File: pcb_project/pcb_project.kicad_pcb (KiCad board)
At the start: 8 copper layers, 238 parts, among them IC1 TPS54325PWPR, IC2 TPS54294PWPR, IC3 IS61WV204816BLL-10TLI, IC4 IS61WV204816BLL-10TLI, J1 Conn_01x10_Pin, J10 M20-9990246, J11 M20-9990246, J12 M20-9990246, J2 FTSH-107-01-F-DV-K, J3 Conn_ST_STDC14, J4 DE15_Socket_HighDensity_Mount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, J5 USB_B_Micro, J6 MEM2052-00-195-00-A, J7 USB_A, J8 M20-9990246, J9 M20-9990246, Q1 BC857BS, Q2 BC847BPN, SW2 SW_SPDT, SW3 SW_SPST, SW4 SW_SPST, U1 XC7A100T-FTG256, U2 STM32U595VJTx, U3 TPS2041B, U4 D3V3XA4B10LP, U7 MAX7221xWG, U8 COM-11405, U9 MT25QL128ABA1ESE-0SIT, Y1 48MHz, Y2 XLH736025.175000I

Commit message: Initial FPGA ballout and vga
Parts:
- C10, C100, C101, C102, C11, C13, C19, C20, C22, C23, C24, C25, C27, C29, C31, C33, C34, C36, C5, C8, C92, C93, C94, C95, C99: footprint Capacitor_SMD:C_0805_2012Metric_Pad1.18x1.45mm_HandSolder -> Capacitor_SMD:C_0603_1608Metric_Pad1.08x0.95mm_HandSolder
- C6: footprint Capacitor_SMD:CP_Elec_10x10.5 -> Capacitor_Tantalum_SMD:CP_EIA-7343-31_Kemet-D_HandSolder
- moved U9 40.8 mm to (86.5, 137.5)
- moved C10 40.2 mm to (64.5, 107.0)
- moved C13 40.2 mm to (69.3, 98.0)
- moved C17 40.2 mm to (69.3, 107.0)
- moved C20 40.2 mm to (74.1, 98.0)
- moved C24 40.2 mm to (74.1, 107.0)
- moved C5 40.2 mm to (64.5, 98.0)
- moved C29 40.2 mm to (78.9, 98.0)
- moved C11 40.2 mm to (69.3, 92.0)
- moved C15 40.2 mm to (69.3, 101.0)
- moved C18 40.2 mm to (74.1, 92.0)
- moved C22 40.2 mm to (74.1, 101.0)
- moved C3 40.2 mm to (64.5, 92.0)
- moved C8 40.2 mm to (64.5, 101.0)
- moved C12 40.2 mm to (69.3, 95.0)
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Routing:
- net /VGA/R0: track 0.00 -> 103.1 mm, vias 0 -> 2
- net /VGA/R1: track 0.00 -> 98.2 mm, vias 0 -> 1
- net /VGA/R2: track 0.00 -> 97.4 mm, vias 0 -> 1
- net /VGA/R3: track 0.00 -> 96.0 mm, vias 0 -> 1
- net /VGA/R4: track 0.00 -> 94.9 mm, vias 0 -> 2
- net /VGA/B3: track 0.00 -> 56.7 mm
- net /VGA/G0: track 0.00 -> 38.2 mm
- net /VGA/B2: track 0.00 -> 36.2 mm
- net /VGA/G1: track 0.00 -> 34.8 mm
- net /VGA/B1: track 0.00 -> 33.5 mm, vias 0 -> 2
- net /VGA/G2: track 0.00 -> 32.8 mm
- net /VGA/G3: track 0.00 -> 32.0 mm
- net /VGA/G4: track 0.00 -> 29.5 mm
- net /VGA/B0: track 0.00 -> 29.4 mm
- net /VGA/G5: track 0.00 -> 28.8 mm
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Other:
- copper layers 8 -> 6

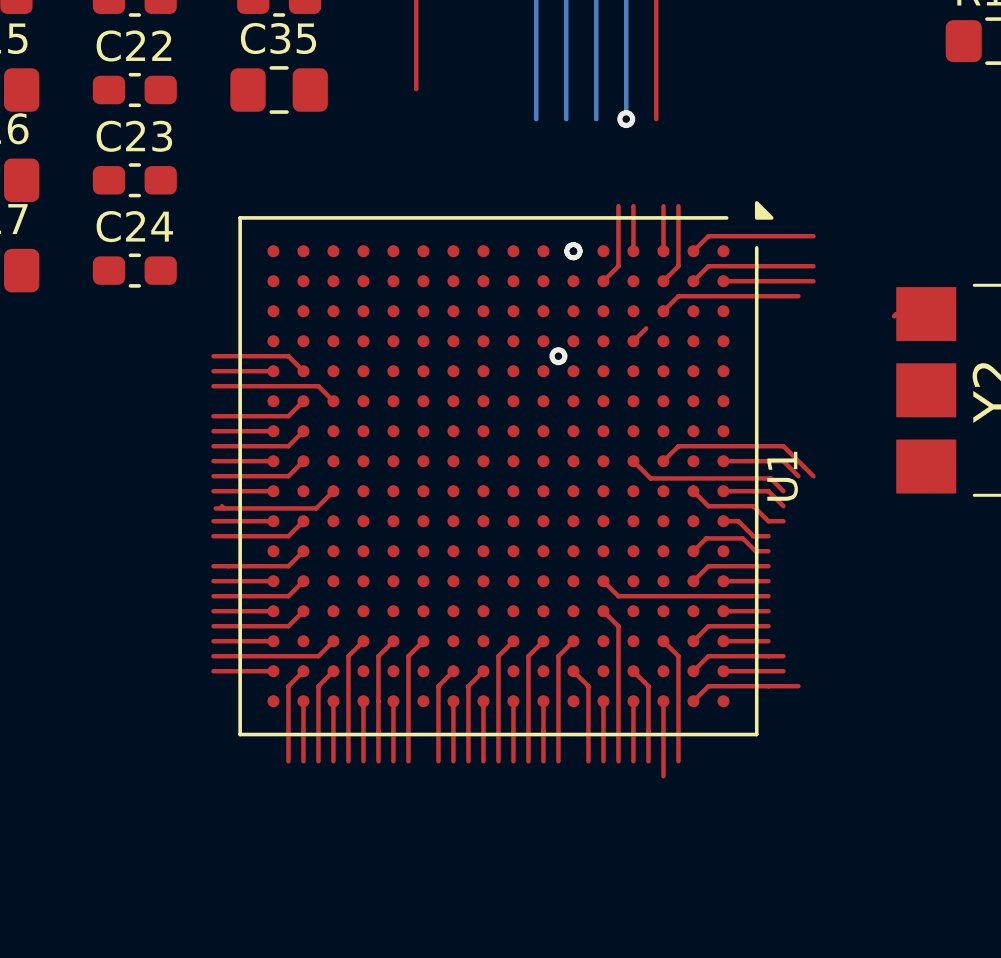
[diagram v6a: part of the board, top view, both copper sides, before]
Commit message: FPGA Dog Bone wires
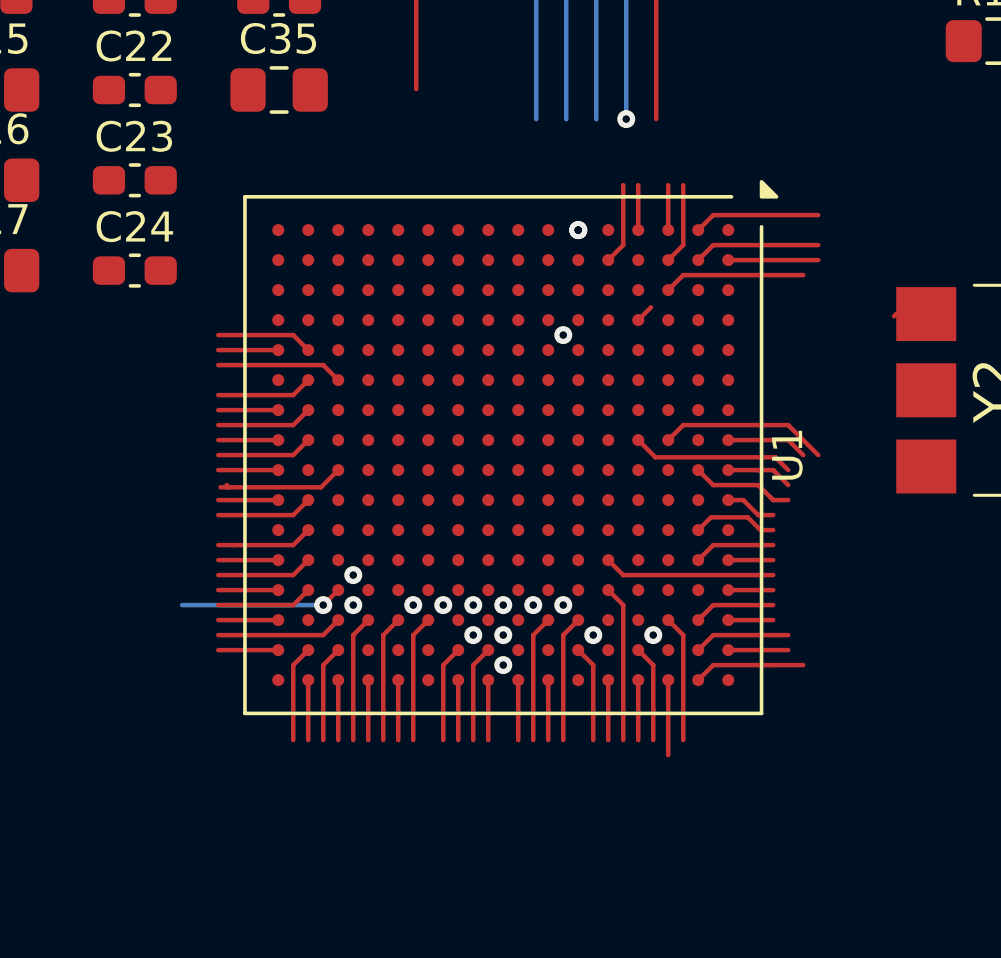
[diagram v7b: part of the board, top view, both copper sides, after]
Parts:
- moved U1 0.72 mm to (86.4, 113.2)
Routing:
- net Net-(IC4-I/O4): track 0.21 -> 5.49 mm, vias 0 -> 1
- net Net-(IC3-I/O15): track 4.21 -> 0.00 mm
- net (no net): vias 1 -> 14

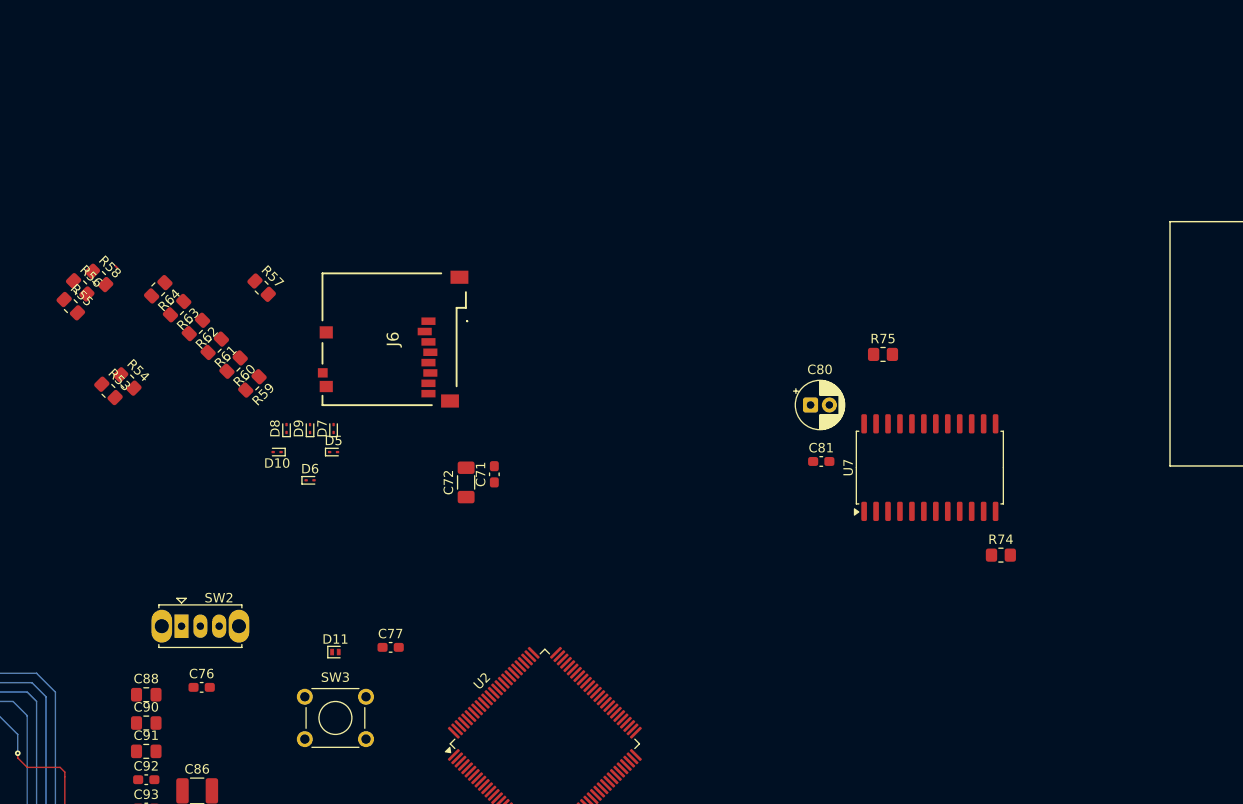
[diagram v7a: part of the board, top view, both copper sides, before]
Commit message: Minor schematic changes for easier Layout
- Proper TVS symbol for MicroSD
- Rename USB data lines net name to allow for differential routing
- Change SDMMC_CD GPIO to easier MCU pin
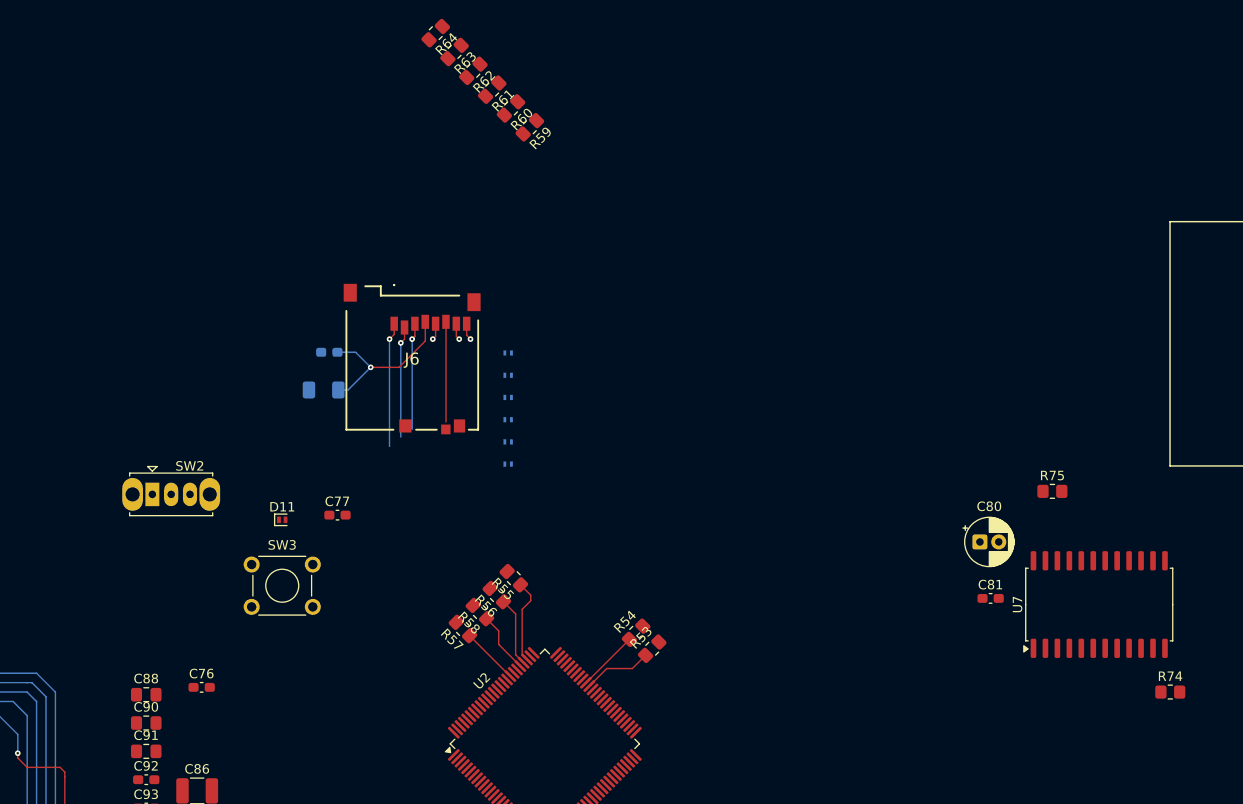
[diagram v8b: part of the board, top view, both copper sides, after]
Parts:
- removed D10, D5, D6, D7, D8, D9: ESD9B3.3ST5G, Diode_SMD:D_SOD-923
- added U10: TPD1E1B04DPYT, Project_Footprints:DPY2_TEX, B.Cu at (138.6, 33.2)
- added U11: TPD1E1B04DPYT, Project_Footprints:DPY2_TEX, B.Cu at (138.6, 35.6)
- added U12: TPD1E1B04DPYT, Project_Footprints:DPY2_TEX, B.Cu at (138.6, 37.9)
- added U13: TPD1E1B04DPYT, Project_Footprints:DPY2_TEX, B.Cu at (138.6, 40.3)
- added U5: TPD1E1B04DPYT, Project_Footprints:DPY2_TEX, B.Cu at (138.6, 28.5)
- added U6: TPD1E1B04DPYT, Project_Footprints:DPY2_TEX, B.Cu at (138.6, 30.8)
- C71, C72: moved to B.Cu
- moved R53 63.9 mm to (153.9, 59.9), turned to 45 degrees
- moved R54 60.3 mm to (152.2, 58.2), turned to 45 degrees
- moved R55 55.2 mm to (139.2, 52.4), turned to 135 degrees
- moved R56 55.0 mm to (137.4, 54.2), turned to 135 degrees
- moved R58 53.8 mm to (135.6, 56.0), turned to 135 degrees
- moved R57 42.1 mm to (133.8, 57.8), turned to 135 degrees
- moved R59 40.1 mm to (140.9, 4.49)
- moved R60 40.1 mm to (138.9, 2.49)
- moved R61 40.1 mm to (136.9, 0.49)
- moved R62 40.1 mm to (134.9, -1.51)
- moved R63 40.1 mm to (132.9, -3.51)
- moved R64 40.1 mm to (130.9, -5.51)
- moved U7 23.1 mm to (201.4, 55.2)
- moved C80 23.1 mm to (188.7, 48.5)
- moved C81 23.1 mm to (189.9, 54.5)
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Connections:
- net /MCU/PA11_OTG_HS_DM(boot) renamed /MCU/OTG_HS_D-
- net /MCU/PA12_OTG_HS_DP(boot) renamed /MCU/OTG_HS_D+
- J6 pad 9: /MCU/PB10_LPGPIO1_P4 -> /MCU/PB4_LPGPIO1_P12
- R59 pad 2: /MCU/PB10_LPGPIO1_P4 -> /MCU/PB4_LPGPIO1_P12
- U2 pad 47: /MCU/PB10_LPGPIO1_P4 -> unconnected-(U2-PB10-Pad47)
- U2 pad 90: unconnected-(U2-PB4-Pad90) -> /MCU/PB4_LPGPIO1_P12
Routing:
- net +3V3: track 0.00 -> 17.6 mm, vias 2 -> 3
- net Net-(J6-DAT2): track 0.00 -> 13.2 mm, vias 0 -> 1
- net Net-(J6-CD/DAT3): track 0.00 -> 12.0 mm, vias 0 -> 1
- net Net-(J6-CMD): track 0.41 -> 11.4 mm, vias 0 -> 1
- net GND: track 0.00 -> 10.6 mm
- net /MCU/PC10_SDMMC1_D2: track 0.00 -> 8.97 mm
- net /MCU/PC11_SDMMC1_D3: track 0.00 -> 7.37 mm
- net /MCU/PC8_SDMMC1_D0: track 0.00 -> 7.33 mm
- net /MCU/PC9_SDMMC1_D1: track 0.00 -> 6.53 mm
- net /MCU/PC12_SDMMC1_CK: track 0.00 -> 6.53 mm
- net /MCU/PD2_SDMMC1_CMD: track 0.00 -> 6.11 mm
- net Net-(J6-DAT1): track 0.00 -> 1.80 mm, vias 0 -> 1
- net Net-(J6-DAT0): track 0.00 -> 1.76 mm, vias 0 -> 1
- net Net-(J6-CLK): track 0.00 -> 1.76 mm, vias 0 -> 1
